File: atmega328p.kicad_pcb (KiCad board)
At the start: 2 copper layers, 68.6 x 53.3 mm, 40 parts, among them CON1 Micro USB, CON2 AVR-ISP-6, IC1 DS3231M, IC2 LD1117, IC3 ATMEGA328-P, M1 D1, P5 CONN_1, P6 CONN_1, P7 CONN_1, P8 CONN_1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

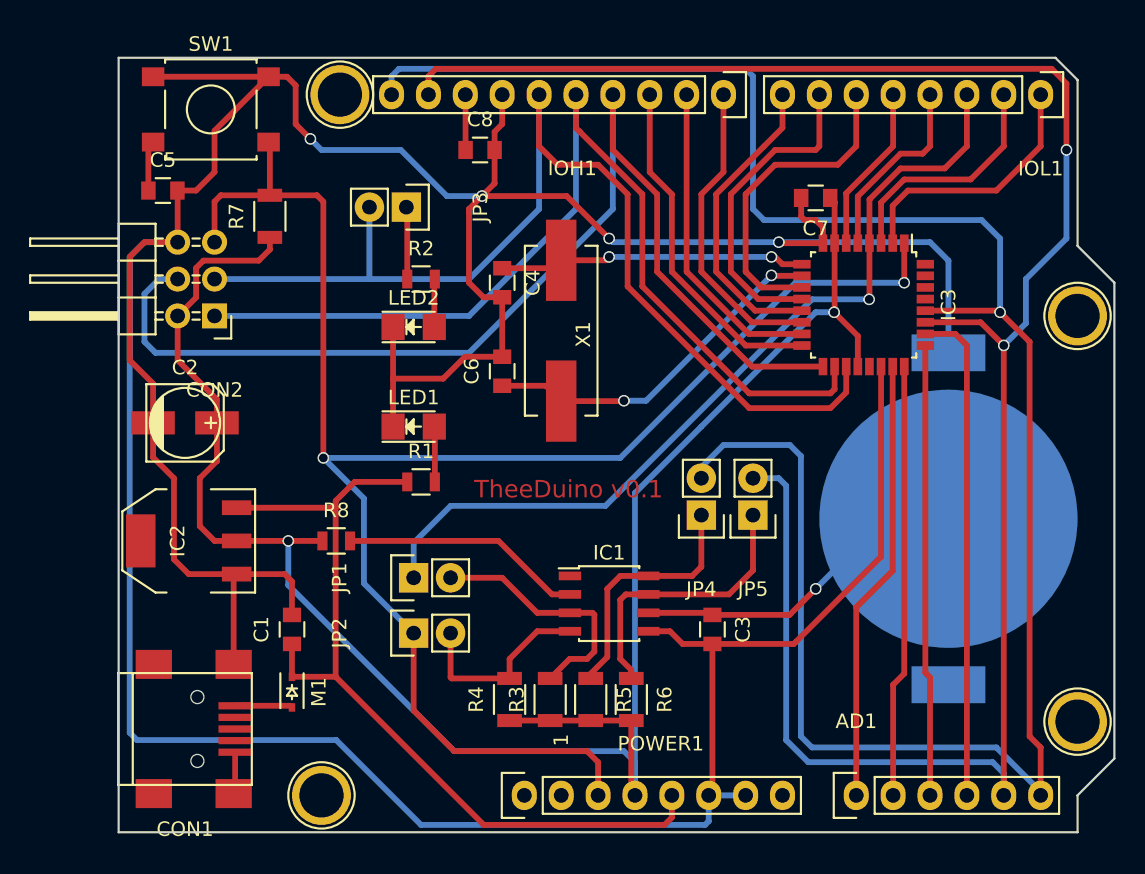
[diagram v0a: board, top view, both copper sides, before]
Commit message: correct wrong footprint and pinout of atmega328p
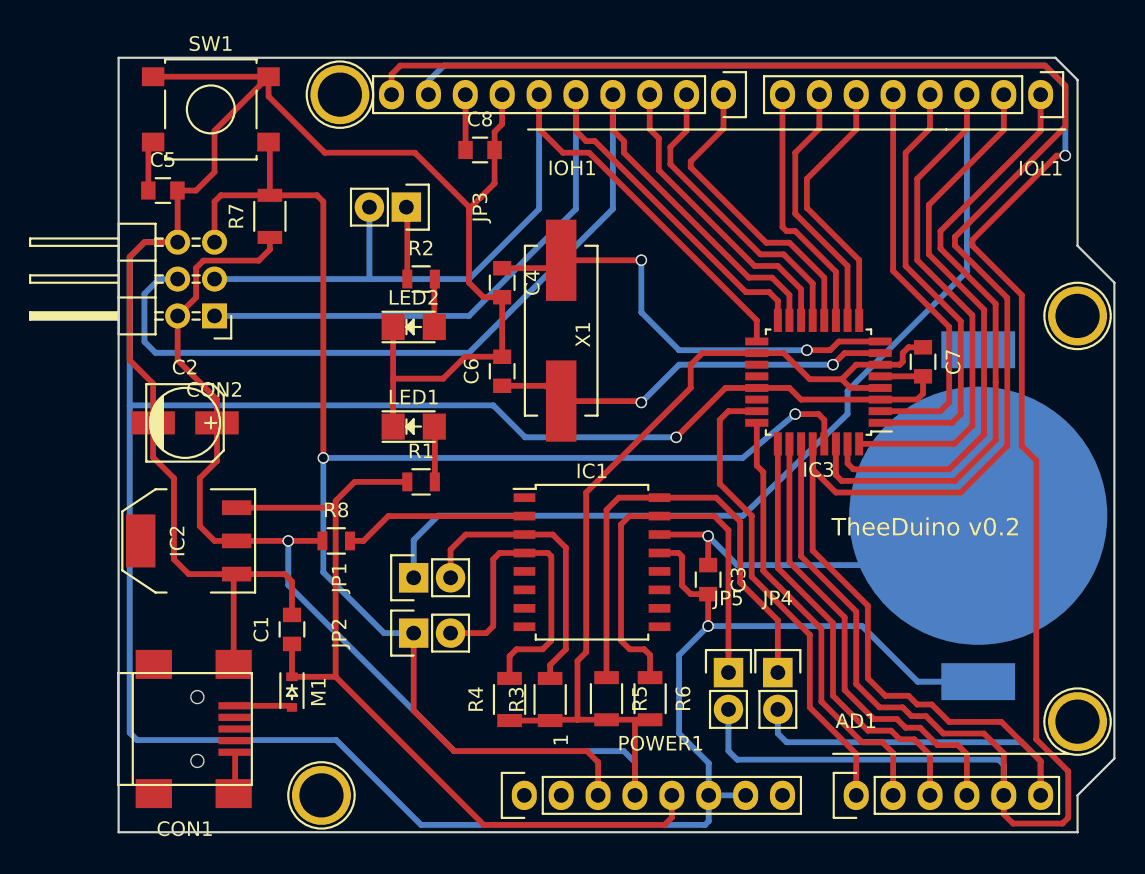
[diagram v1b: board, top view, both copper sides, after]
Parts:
- IC1: value DS3231M -> DS3231M_SO16; footprint Housings_SOIC:SOIC-8_3.9x4.9mm_Pitch1.27mm -> Housings_SOIC:SOIC-16W_7.5x10.3mm_Pitch1.27mm
- IC3: value ATMEGA328-P -> ATMEGA328P-TQFP32; footprint Housings_QFP:LQFP-32_7x7mm_Pitch0.8mm -> Housings_QFP:TQFP-32_7x7mm_Pitch0.8mm
- moved C7 13.5 mm to (166.4, 94.0), turned to 270 degrees
- moved JP4 12.1 mm to (156.4, 115.4), turned to 0 degrees
- moved JP5 11.0 mm to (153.0, 115.4), turned to 0 degrees
- moved IC3 6.16 mm to (159.2, 95.4), turned to 180 degrees
- moved C3 3.44 mm to (151.6, 109.0)
- moved IC1 3.09 mm to (143.6, 107.8)
- moved BATT1 2.06 mm to (170.2, 104.6)
- moved R6 1.30 mm to (147.6, 117.2)
- moved R5 1.09 mm to (144.6, 117.2)
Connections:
- BATT1 pad 2: GND -> (no net)
- IC1 pad 5: GND -> Net-(IC1-Pad5)
- IC1 pad 6: Net-(BATT1-Pad1) -> Net-(IC1-Pad6)
- IC3 pad 1: RST -> Net-(IC3-Pad1)
- IC3 pad 10: Net-(C6-Pad1) -> Net-(IC3-Pad10)
- IC3 pad 15: Net-(IC3-Pad15) -> Net-(CON2-Pad4)
- IC3 pad 16: Net-(IC3-Pad16) -> Net-(CON2-Pad1)
- IC3 pad 17: Net-(CON2-Pad4) -> PB5
- IC3 pad 18: Net-(CON2-Pad1) -> +3V3
- IC3 pad 19: PB5 -> Net-(IC3-Pad19)
- IC3 pad 20: +3V3 -> AREF
- IC3 pad 21: AREF -> GND
- IC3 pad 22: GND -> Net-(IC3-Pad22)
- IC3 pad 29: (no net) -> RST
- IC3 pad 3: Net-(IC3-Pad3) -> GND
- IC3 pad 30: (no net) -> Net-(IC3-Pad30)
- IC3 pad 31: (no net) -> Net-(IC3-Pad31)
- IC3 pad 32: (no net) -> INT0
- IC3 pad 4: INT0 -> +3V3
- IC3 pad 5: Net-(IC3-Pad5) -> GND
- IC3 pad 6: Net-(IC3-Pad6) -> +3V3
- IC3 pad 7: +3V3 -> Net-(C6-Pad1)
- IC3 pad 8: GND -> Net-(C4-Pad1)
- IC3 pad 9: Net-(C4-Pad1) -> Net-(IC3-Pad9)
- IOH1 pad 1: Net-(IC3-Pad14) -> Net-(IC3-Pad12)
- IOH1 pad 2: Net-(IC3-Pad15) -> Net-(IC3-Pad13)
- IOH1 pad 3: Net-(IC3-Pad16) -> Net-(IC3-Pad14)
- IOL1 pad 1: Net-(IC3-Pad2) -> Net-(IC3-Pad30)
- IOL1 pad 2: Net-(IC3-Pad3) -> Net-(IC3-Pad31)
- IOL1 pad 4: Net-(IC3-Pad5) -> Net-(IC3-Pad1)
- IOL1 pad 5: Net-(IC3-Pad6) -> Net-(IC3-Pad2)
- IOL1 pad 6: Net-(IC3-Pad11) -> Net-(IC3-Pad9)
- IOL1 pad 7: Net-(IC3-Pad12) -> Net-(IC3-Pad10)
- IOL1 pad 8: Net-(IC3-Pad13) -> Net-(IC3-Pad11)
- JP4 pad 1: Net-(IC1-Pad8) -> Net-(IC1-Pad16)
- JP5 pad 1: Net-(IC1-Pad7) -> Net-(IC1-Pad15)
- R5 pad 1: Net-(IC1-Pad8) -> Net-(IC1-Pad16)
- R6 pad 1: Net-(IC1-Pad7) -> Net-(IC1-Pad15)
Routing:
- net Net-(IC3-Pad30): track 0.00 -> 43.1 mm
- net Net-(IC3-Pad31): track 0.00 -> 39.0 mm
- net INT0: track 59.6 -> 95.5 mm, vias 1 -> 0
- net Net-(IC1-Pad16): track 0.00 -> 33.3 mm
- net Net-(IC3-Pad1): track 0.00 -> 30.1 mm
- net Net-(IC1-Pad15): track 0.00 -> 29.8 mm
- net SDA: track 140.2 -> 165.6 mm, vias 2 -> 1
- net Net-(IC3-Pad16): track 23.9 -> 0.00 mm
- net Net-(IC3-Pad15): track 21.9 -> 0.00 mm
- net Net-(IC1-Pad7): track 19.5 -> 0.00 mm
- net Net-(IC3-Pad9): track 0.00 -> 18.4 mm
- net Net-(IC3-Pad10): track 0.00 -> 17.7 mm
- net Net-(IC1-Pad8): track 17.4 -> 0.00 mm
- net Net-(IC3-Pad3): track 16.4 -> 0.00 mm
- net PB5: track 75.3 -> 61.4 mm
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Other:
- board text added: "TheeDuino v0.2"
- board text removed: "TheeDuino v0.1"
